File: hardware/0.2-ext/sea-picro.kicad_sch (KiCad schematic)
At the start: 59 parts, among them J1 USB_C_Receptacle_USB2.0, J2 0.1" x 12, J3 0.1" x 12, J4 D+, J5 D-, J6 0.1" x 5, J7 2.54, Q1 2N7002VC-7, Q2 2N7002VC-7, U1 ME6211C33M5G-N, U2 GD25Q64CWIGR, U3 RP2040, U4 74LVC1T45Z6-7, Y1 12MHz

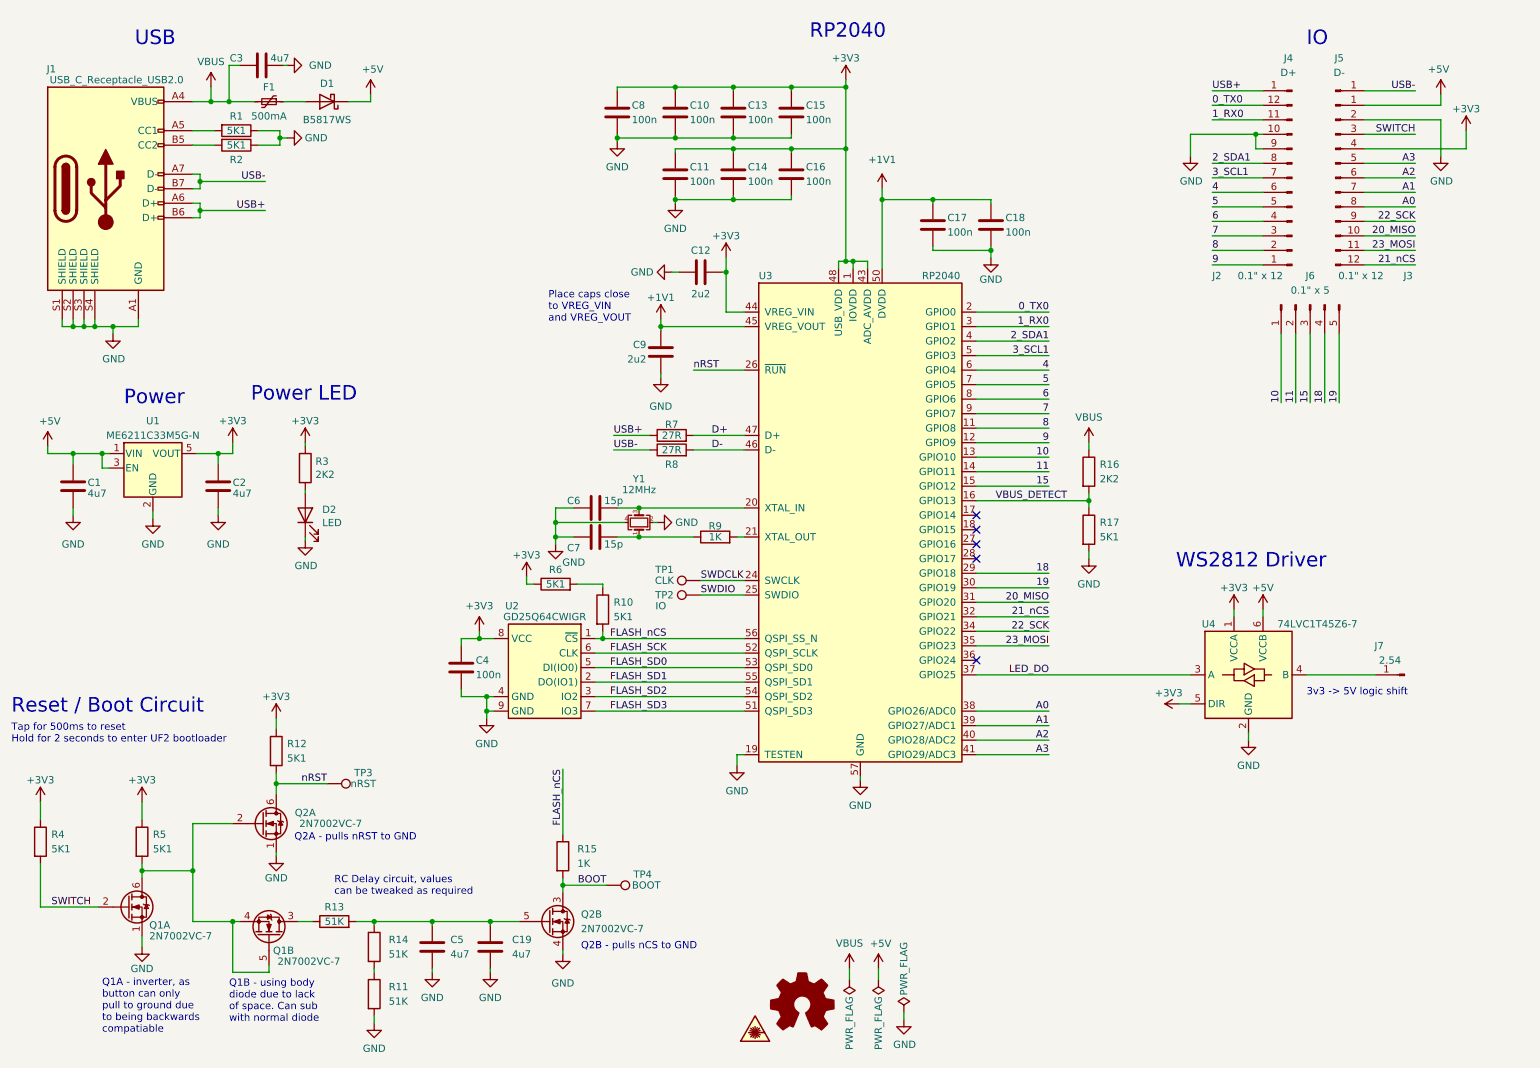
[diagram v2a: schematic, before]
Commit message: update ldo caps to 1u
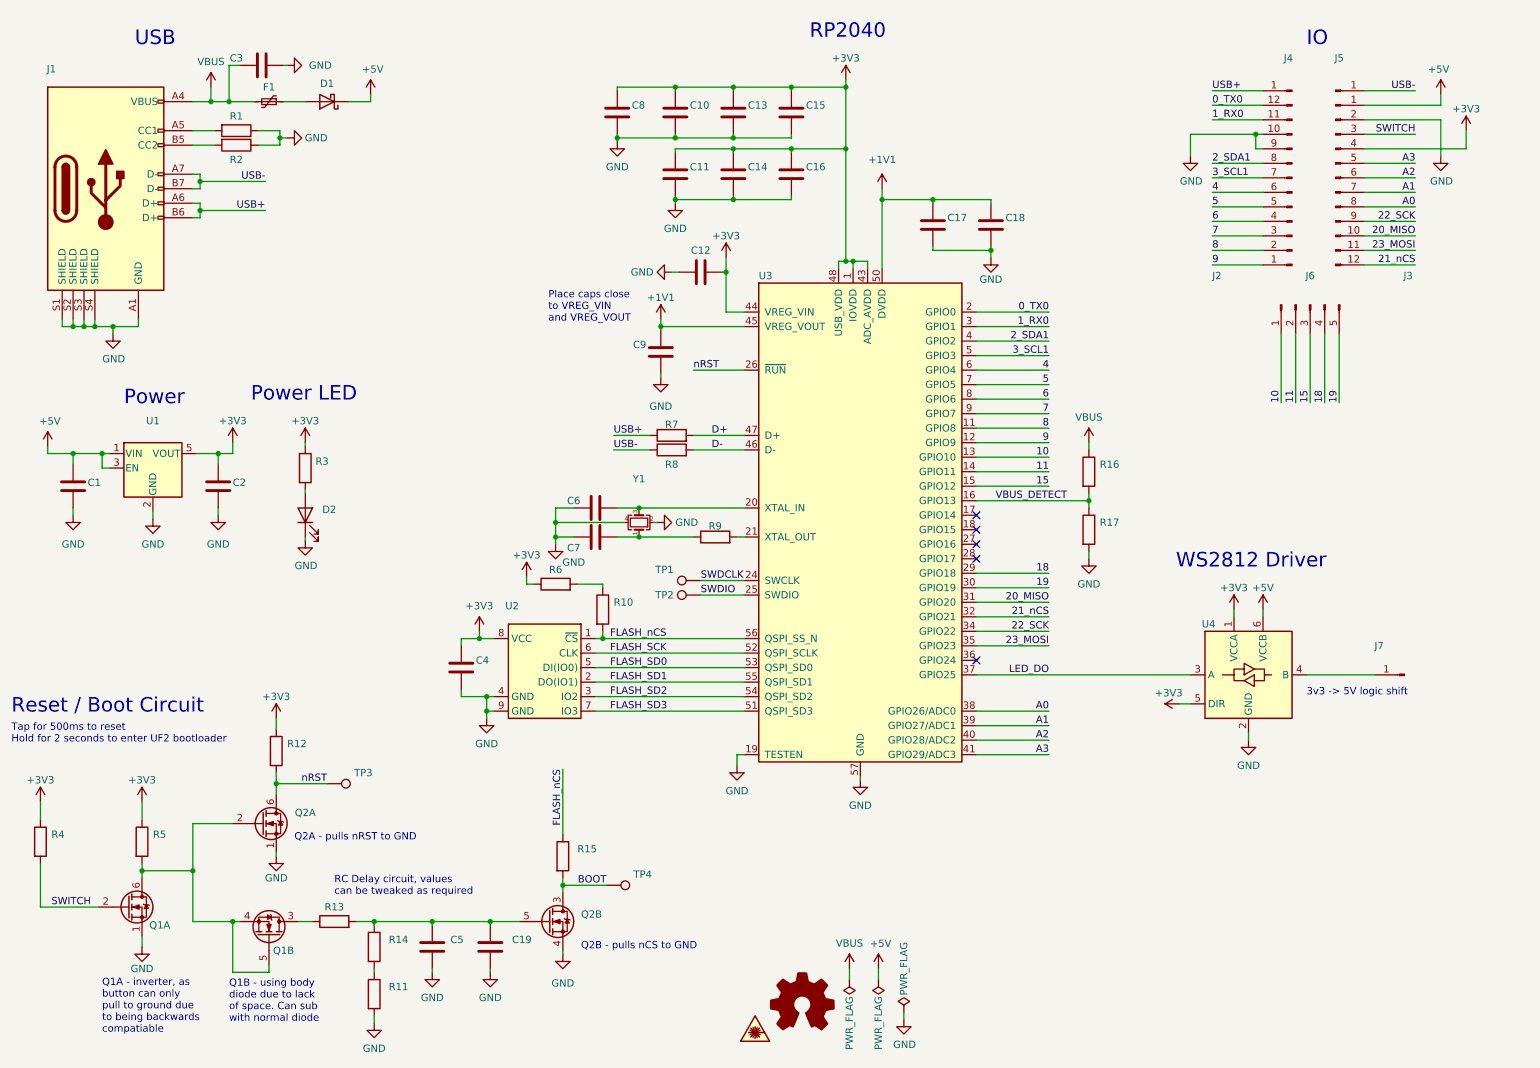
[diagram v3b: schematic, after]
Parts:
- C1, C19, C2, C3, C5: value 4u7 -> (none); footprint Capacitor_SMD:C_0402_1005Metric -> (none)
- C10, C11, C13, C14, C15, C16, C17, C18, C4, C8: value 100n -> (none); footprint Capacitor_SMD:C_0402_1005Metric -> (none)
- C12, C9: value 2u2 -> (none); footprint Capacitor_SMD:C_0402_1005Metric -> (none); LCSC C12530 -> C15849; MPN  CL05A225MQ5NSNC -> CL10A105KB8NNNC
- C6, C7: value 15p -> (none); footprint Capacitor_SMD:C_0402_1005Metric -> (none)
- D1: value B5817WS -> (none); footprint Diode_SMD:D_SOD-323 -> (none)
- D2: value LED -> (none); footprint LED_SMD:LED_0603_1608Metric -> (none)
- F1: value 500mA -> (none); footprint josh-passives-smt:Fuse_0603_1608Metric -> (none)
- J1: value USB_C_Receptacle_USB2.0 -> (none); footprint josh-connectors:USB-C_MID_MOUNT_918-418K2024S40000 -> (none)
- J2, J3: value 0.1" x 12 -> (none); footprint josh-connectors:Castellated_Short_P2.54x12 -> (none)
- J4: value D+ -> (none); footprint josh-connectors:PinHeader_1x01_P2.54mm_Circle -> (none)
- J5: value D- -> (none); footprint josh-connectors:PinHeader_1x01_P2.54mm_Circle -> (none)
- J6: value 0.1" x 5 -> (none); footprint josh-connectors:PinHeader_1x05_P2.54mm_Circle -> (none)
- J7: value 2.54 -> (none); footprint josh-connectors:PinHeader_1x01_P2.54mm_Circle -> (none)
- LOGO1: value Logo_Open_Hardware_Small -> (none); footprint josh-logos:OSHW_Logo_3.6x3.6_F.Mask -> (none)
- LOGO2: value Sea-Picro -> (none); footprint josh-logos:sea-picro-silk -> (none)
- Q1, Q2: value 2N7002VC-7 -> (none); footprint Package_TO_SOT_SMD:SOT-563 -> (none)
- R1, R10, R12, R17, R2, R4, R5, R6: value 5K1 -> (none); footprint Resistor_SMD:R_0402_1005Metric -> (none)
- R11, R13, R14: value 51K -> (none); footprint Resistor_SMD:R_0402_1005Metric -> (none)
- R15, R9: value 1K -> (none); footprint Resistor_SMD:R_0402_1005Metric -> (none)
- R16, R3: value 2K2 -> (none); footprint Resistor_SMD:R_0402_1005Metric -> (none)
- R7, R8: value 27R -> (none); footprint Resistor_SMD:R_0402_1005Metric -> (none)
- TP1: value CLK -> (none); footprint josh-test-point:TestPoint_THTPad_D1.0mm_Drill0.5mm_NO_SILK -> (none)
- TP2: value IO -> (none); footprint josh-test-point:TestPoint_THTPad_D1.0mm_Drill0.5mm_NO_SILK -> (none)
- TP3: value nRST -> (none); footprint josh-test-point:TestPoint_SMDPad_D1.0mm_NO_SILK -> (none)
- TP4: value BOOT -> (none); footprint josh-test-point:TestPoint_SMDPad_D1.0mm_NO_SILK -> (none)
- U1: value ME6211C33M5G-N -> (none); footprint Package_TO_SOT_SMD:SOT-23-5 -> (none)
- U2: value GD25Q64CWIGR -> (none); footprint Package_SON:WSON-8-1EP_6x5mm_P1.27mm_EP3.4x4mm -> (none)
- U3: value RP2040 -> (none); footprint josh-dfn-qfn:RP2040-QFN-56 -> (none)
- U4: value 74LVC1T45Z6-7 -> (none); footprint Package_TO_SOT_SMD:SOT-563 -> (none)
- Y1: value 12MHz -> (none); footprint josh-oscillators:Crystal_SMD_2520-4Pin_2.5x2.0mm -> (none)

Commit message: fixes after assembly
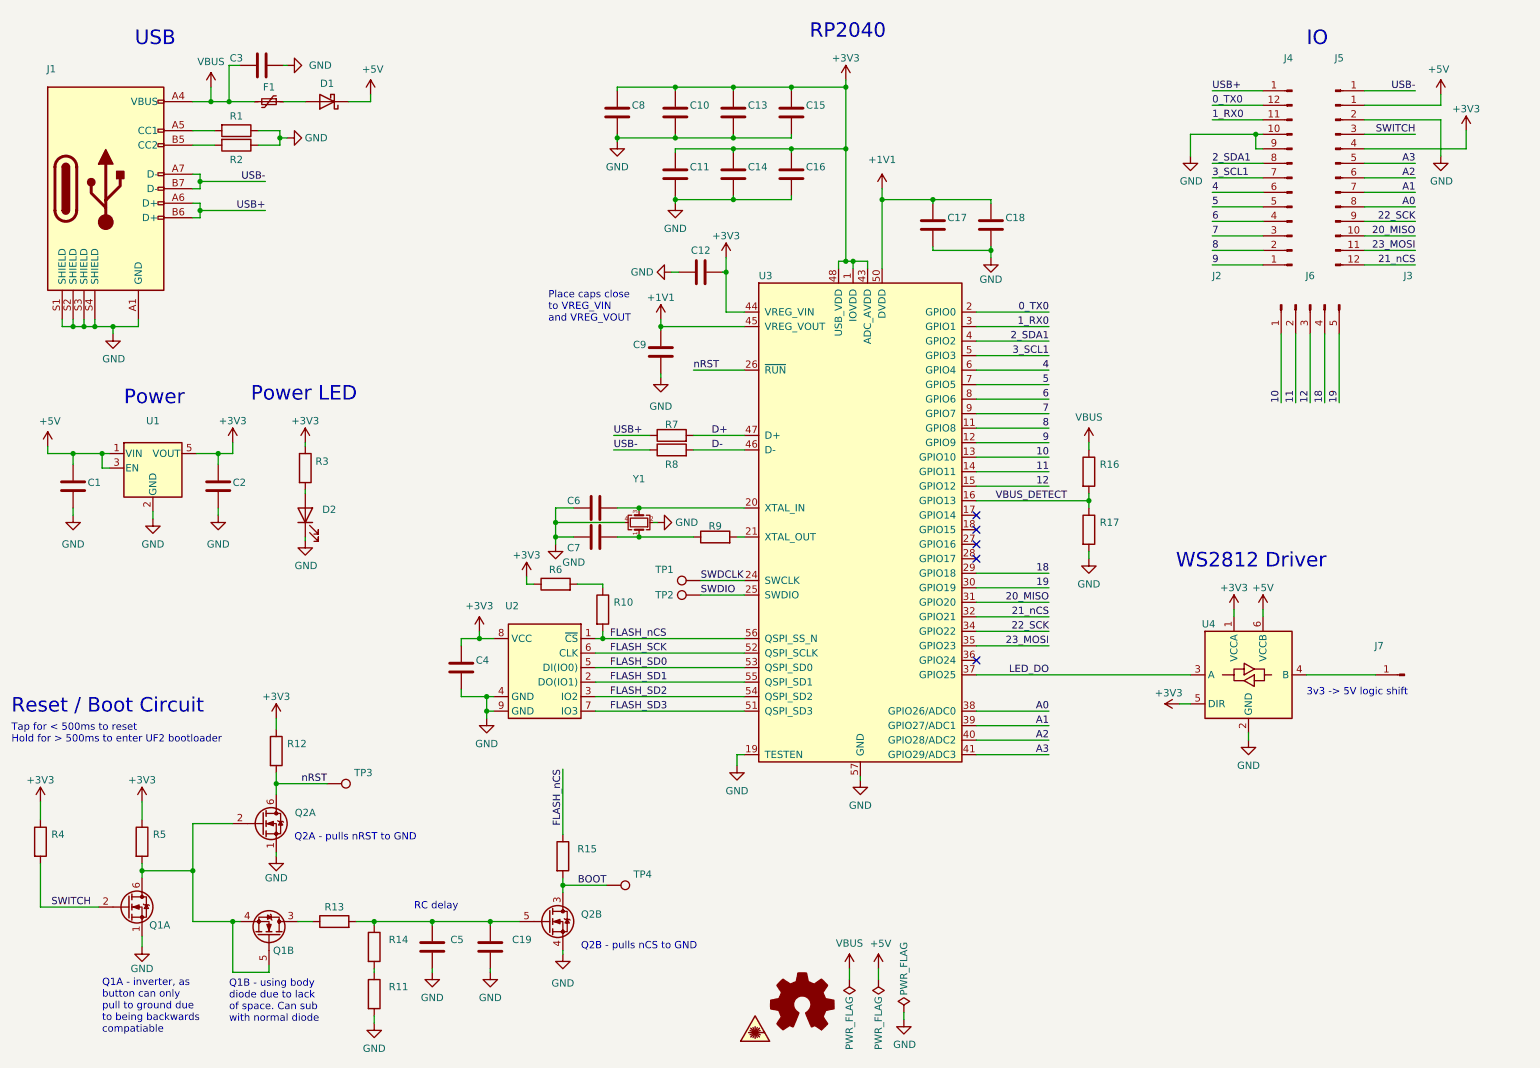
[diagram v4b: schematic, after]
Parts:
- U1: LCSC C82942 -> C150742; MPN  ME6211C33M5G-N -> AP7365-33WG-7; Manufacturer MICRONE(Nanjing Micro One Elec) -> Diodes Incorporated
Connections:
- net 15 renamed 12
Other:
- note added: "RC delay"
- note added: "Tap for < 500ms to reset Hold for > 500ms to enter UF2 bootloader"
- note removed: "RC Delay circuit, values can be tweaked as required"
- note removed: "Tap for 500ms to reset Hold for 2 seconds to enter UF2 bootloader"
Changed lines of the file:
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@@
     (effects (font (size 1.27 1.27)) (justify left bottom))
   )
-  (text "Tap for 500ms to reset\nHold for 2 seconds to enter UF2 bootloader"
+  (text "Tap for < 500ms to reset\nHold for > 500ms to enter UF2 bootloader"
     (at 17.78 143.51 0)
     (effects (font (size 1.27 1.27)) (justify left bottom))
   )
-  (text "RC Delay circuit, values\ncan be tweaked as required"
-    (at 74.295 170.18 0)
+  (text "RC delay" (at 88.265 172.72 0)
     (effects (font (size 1.27 1.27)) (justify left bottom))
   )
@@
     (effects (font (size 1.27 1.27)) (justify right bottom))
   )
-  (label "15" (at 199.39 98.425 180)
+  (label "12" (at 199.39 98.425 180)
     (effects (font (size 1.27 1.27)) (justify right bottom))
   )
@@
     (effects (font (size 1.27 1.27)) (justify right bottom))
   )
-  (label "15" (at 245.11 83.82 90)
+  (label "12" (at 245.11 83.82 90)
     (effects (font (size 1.27 1.27)) (justify left bottom))
   )
@@
       (effects (font (size 1.27 1.27)) hide)
     )
-    (property "LCSC" "C82942" (id 4) (at 42.545 95.25 0)
-      (effects (font (size 1.27 1.27)) hide)
-    )
-    (property "MPN " "ME6211C33M5G-N" (id 5) (at 42.545 95.25 0)
-      (effects (font (size 1.27 1.27)) hide)
-    )
-    (property "Manufacturer" "MICRONE(Nanjing Micro One Elec)" (id 6) (at 42.545 95.25 0)
+    (property "LCSC" "C150742" (id 4) (at 42.545 95.25 0)
+      (effects (font (size 1.27 1.27)) hide)
+    )
+    (property "MPN " "AP7365-33WG-7 " (id 5) (at 42.545 95.25 0)
+      (effects (font (size 1.27 1.27)) hide)
+    )
+    (property "Manufacturer" "Diodes Incorporated" (id 6) (at 42.545 95.25 0)
       (effects (font (size 1.27 1.27)) hide)
     )
@@
     )
     (path "/d26fce45-c1d6-42bc-931d-972bf3799097"
-      (reference "U1") (unit 1) (value "ME6211C33M5G-N") (footprint "Package_TO_SOT_SMD:SOT-23-5")
+      (reference "U1") (unit 1) (value "AP7365-33WG-7 ") (footprint "Package_TO_SOT_SMD:SOT-23-5")
     )
     (path "/578f7d98-6025-491f-b2c7-18b0b10fb26e"

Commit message: fix lcsc pn typo
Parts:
- Y1: LCSC C2C2149204149205 -> C2149204
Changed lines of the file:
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@@
       (effects (font (size 1.27 1.27)) hide)
     )
-    (property "LCSC" "C2C2149204149205" (id 4) (at 127.635 104.775 0)
+    (property "LCSC" "C2149204" (id 4) (at 127.635 104.775 0)
       (effects (font (size 1.27 1.27)) hide)
     )
